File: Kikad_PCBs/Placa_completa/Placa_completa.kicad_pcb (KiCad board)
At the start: 2 copper layers, 200 x 61.1 mm, 57 parts, among them J1 Conn_01x03, J2 Vo+, J3 VoGnd, Q1 FQP5N60C, T1 Transformer_1P_2S, U1 UC2844N, U2 PC817, U3 TL431

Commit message: modificaciones al pcb
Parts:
- removed D2: 20V, Diodes_THT:D_DO-41_SOD81_P7.62mm_Horizontal
- removed D4: Daux, Diodes_THT:D_DO-41_SOD81_P7.62mm_Horizontal
- removed TH1: NTC, Capacitors_ThroughHole:C_Disc_D16.0mm_W5.0mm_P7.50mm
- added DZ1: 20V, Diodes_THT:D_DO-41_SOD81_P7.62mm_Horizontal, F.Cu at (180.7, 71.8)
- added Daux1: N1106, TO_SOT_Packages_THT:TO-220-2_Vertical, F.Cu at (177.9, 62.8)
- added J4: N, Pin_Headers:Pin_Header_Straight_1x01_Pitch2.54mm, F.Cu at (44.7, 78.4)
- added J5: Earth, Pin_Headers:Pin_Header_Straight_1x01_Pitch2.54mm, F.Cu at (44.8, 86.0)
- added NTC1: I5D20R, Capacitors_ThroughHole:C_Disc_D16.0mm_W5.0mm_P7.50mm, F.Cu at (92.2, 42.4)
- C1: value 1u -> 0.1u
- C5: value 1.8p -> 1.5n
- Cout1: value 380u -> 330u
- Csnubb1: value 47n -> 39p
- Cy2: value 100N -> 100n
- Dsec1, Dsec2: value MUR860 -> BYV29X
- Dsnub1: value D -> HER205
- J1: value Conn_01x03 -> L; footprint Pin_Headers:Pin_Header_Straight_1x03_Pitch2.54mm -> Pin_Headers:Pin_Header_Straight_1x01_Pitch2.54mm
- Q1: value FQP5N60C -> FQP8N60C
- R3: value 768 -> 4k7
- R4: value 4.75M -> 4k7
- RV1: value 5k -> 1k
- Raux1: value 9.76 -> 1k
- Rbledder1: value 22k -> 10K
- Rcs1: value 4k2 -> 3K9
- Rstartup1, Rstartup2: value 75k -> 82K
- Rt1: value 13.7k -> 15k
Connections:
- PTC1 pad 2: Earth -> Net-(PTC1-Pad2)
- RV1 pad 3: Net-(PTC1-Pad1) -> Net-(PTC1-Pad2)
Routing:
- net Earth_Protective: track 49.0 -> 5.45 mm
- net Earth: track 300.6 -> 332.7 mm
- net Net-(Daux1-Pad2): track 45.4 -> 57.3 mm
- net GNDPWR: track 44.0 -> 35.0 mm
- net Net-(PTC1-Pad2): track 0.00 -> 5.77 mm
- net Net-(Daux1-Pad1): track 20.0 -> 14.4 mm
- net Net-(PTC1-Pad1): track 22.7 -> 18.0 mm
- removed copper zone on B.Cu, net GNDPWR
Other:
- outline, holes or cut-outs redrawn

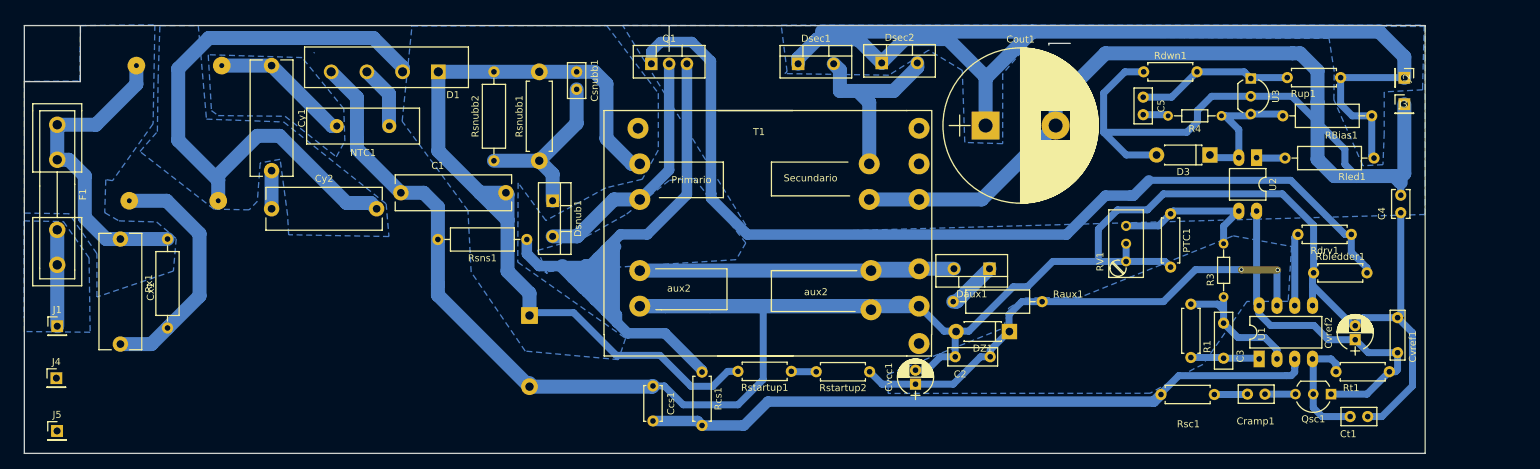
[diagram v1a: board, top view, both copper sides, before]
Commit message: cambio proyecto kicad por el que usamos en la primer fuente completa y modificacion de tamaños, bordes rellenos adaptado a la placa final. Falta ver que queden bien las serigrafias y modificar los componentes qe hizo el riojano para que queden todas las serigrafias bien
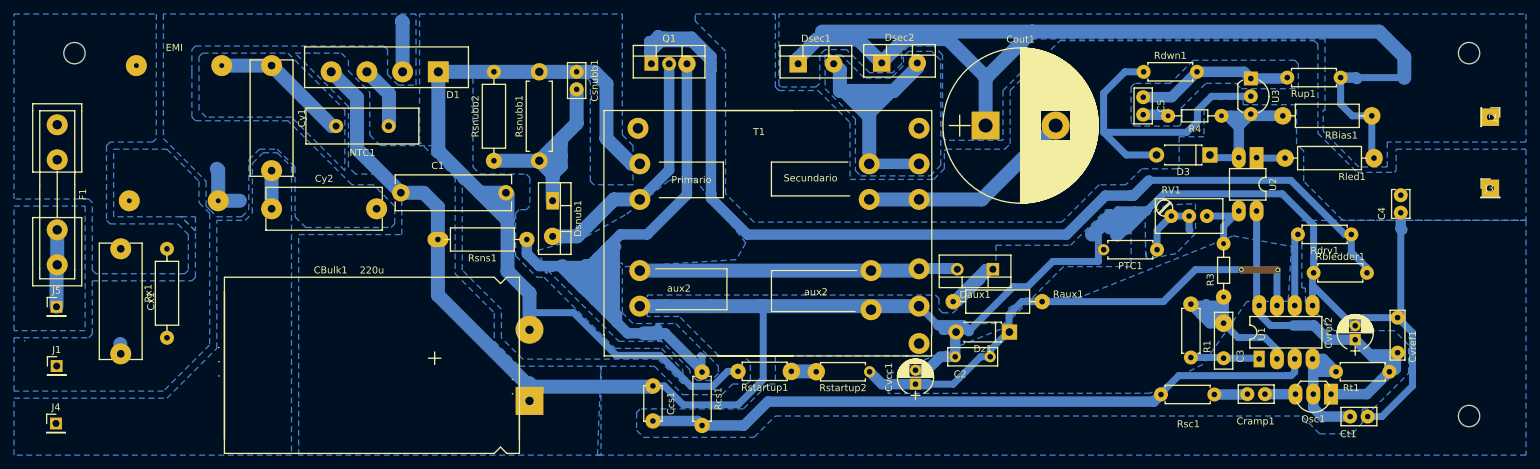
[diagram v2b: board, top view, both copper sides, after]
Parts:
- removed DZ1: 20V, Diodes_THT:D_DO-41_SOD81_P7.62mm_Horizontal
- added Dz1: 20V, Diodes_THT:D_DO-41_SOD81_P7.62mm_Horizontal, F.Cu at (180.7, 71.8)
- CBulk1: moved to F.Cu
- Cy2: value 100n -> 100N
- Dsnub1: value HER205 -> D
- J1: value L -> N
- J4: value N -> Earth
- J5: value Earth -> L
- Rbledder1: value 10K -> 22k
- Rcs1: value 3K9 -> 3k9
- moved J5 17.7 mm to (44.7, 68.2)
- moved J3 17.2 mm to (249.4, 51.3)
- moved J2 13.5 mm to (249.4, 41.1)
- moved RV1 9.14 mm to (203.9, 55.3), turned to 180 degrees
- moved J4 6.48 mm to (44.6, 84.9)
- moved J1 5.69 mm to (44.7, 76.7)
- moved PTC1 5.48 mm to (201.8, 60.1), turned to 180 degrees
- moved Rx1 1.40 mm to (60.5, 72.6)
- moved Cx1 1.40 mm to (53.8, 59.9)
- moved Daux1 0.49 mm to (178.4, 62.9)
- moved NTC1 0.10 mm to (92.1, 42.4)
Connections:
- J1 pad 1: VAC -> GNDPWR
- J4 pad 1: GNDPWR -> Earth_Protective
- J5 pad 1: Earth_Protective -> VAC
- PTC1 pad 2: Net-(PTC1-Pad2) -> Earth
- R3 pad 2: Net-(PTC1-Pad1) -> Net-(R3-Pad2)
- RV1 pad 1: Earth -> Net-(PTC1-Pad1)
- RV1 pad 2: Earth -> Net-(PTC1-Pad1)
- RV1 pad 3: Net-(PTC1-Pad2) -> Net-(R3-Pad2)
- U2 pad 3: Net-(PTC1-Pad1) -> Net-(R3-Pad2)
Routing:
- net GND: track 181.2 -> 76.5 mm
- net Net-(Cy2-Pad2): track 87.5 -> 15.7 mm
- net Net-(Cx1-Pad1): track 45.3 -> 0.00 mm
- net GNDPWR: track 35.0 -> 0.02 mm
- net Net-(Dsec1-Pad2): track 28.4 -> 54.0 mm
- net /Etapa de control/Gate: track 202.7 -> 222.5 mm
- net Net-(Cvref1-Pad2): track 52.5 -> 71.0 mm
- net Net-(C3-Pad2): track 19.3 -> 35.6 mm
- net Net-(D3-Pad1): track 20.6 -> 36.2 mm
- net Earth: track 332.7 -> 318.7 mm
- net Net-(Ct1-Pad2): track 17.9 -> 30.4 mm
- net Net-(C5-Pad1): track 22.5 -> 34.2 mm
- net Net-(Csnubb1-Pad2): track 25.4 -> 36.4 mm
- net Net-(R3-Pad2): track 0.00 -> 10.5 mm
- net Net-(PTC1-Pad1): track 18.0 -> 10.3 mm
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- added copper zone on B.Cu, net Earth_Protective
- added copper zone on B.Cu, net GNDPWR
- added copper zone on B.Cu, net Net-(Dsec1-Pad2)
- added copper zone on B.Cu, net Net-(PTC1-Pad1)
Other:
- board size 200 x 61.1 mm -> 202.2 x 54.9 mm

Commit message: Placa completa terminada por jose, falta revision de los chicos
corregidas las serigrafias, estan todas en la capa top y las pistas. hay que revisar de nuevo los tamaños para que entre bien en la carcasa, averiguar com es lo de los huecos y si tiene que tener marcas de alineacion para mandar a fabricar. los gerber no estan hechos.
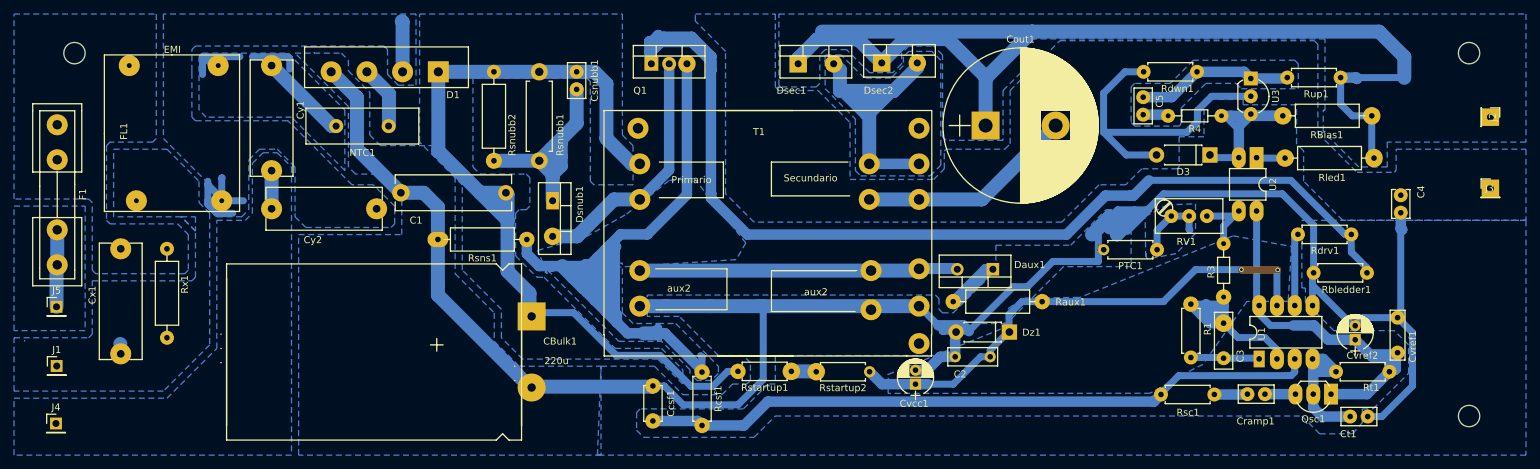
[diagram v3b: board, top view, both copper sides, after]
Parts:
- Cy2: value 100N -> 100n
- FL1: moved to F.Cu
- moved CBulk1 1.93 mm to (112.5, 73.7)
- turned FL1 to 90 degrees
- renumbered Ccs1 to Ccsf1, Rcs1 to Rcsf1
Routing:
- net Net-(Cy2-Pad2): track 15.7 -> 28.7 mm
- net Net-(Cy1-Pad1): track 20.0 -> 32.0 mm
